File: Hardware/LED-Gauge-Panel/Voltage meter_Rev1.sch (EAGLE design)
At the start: 32 parts, among them J1 SL04, Q1 MOSFET-PCHANNEL, Q2 MOSFET-PCHANNEL, Q3 MOSFET-PCHANNEL, U1 ATMEGA328P_PDIPDIL28-4, U2 MAX232D, X1 22-23-2031, X2 16MHz

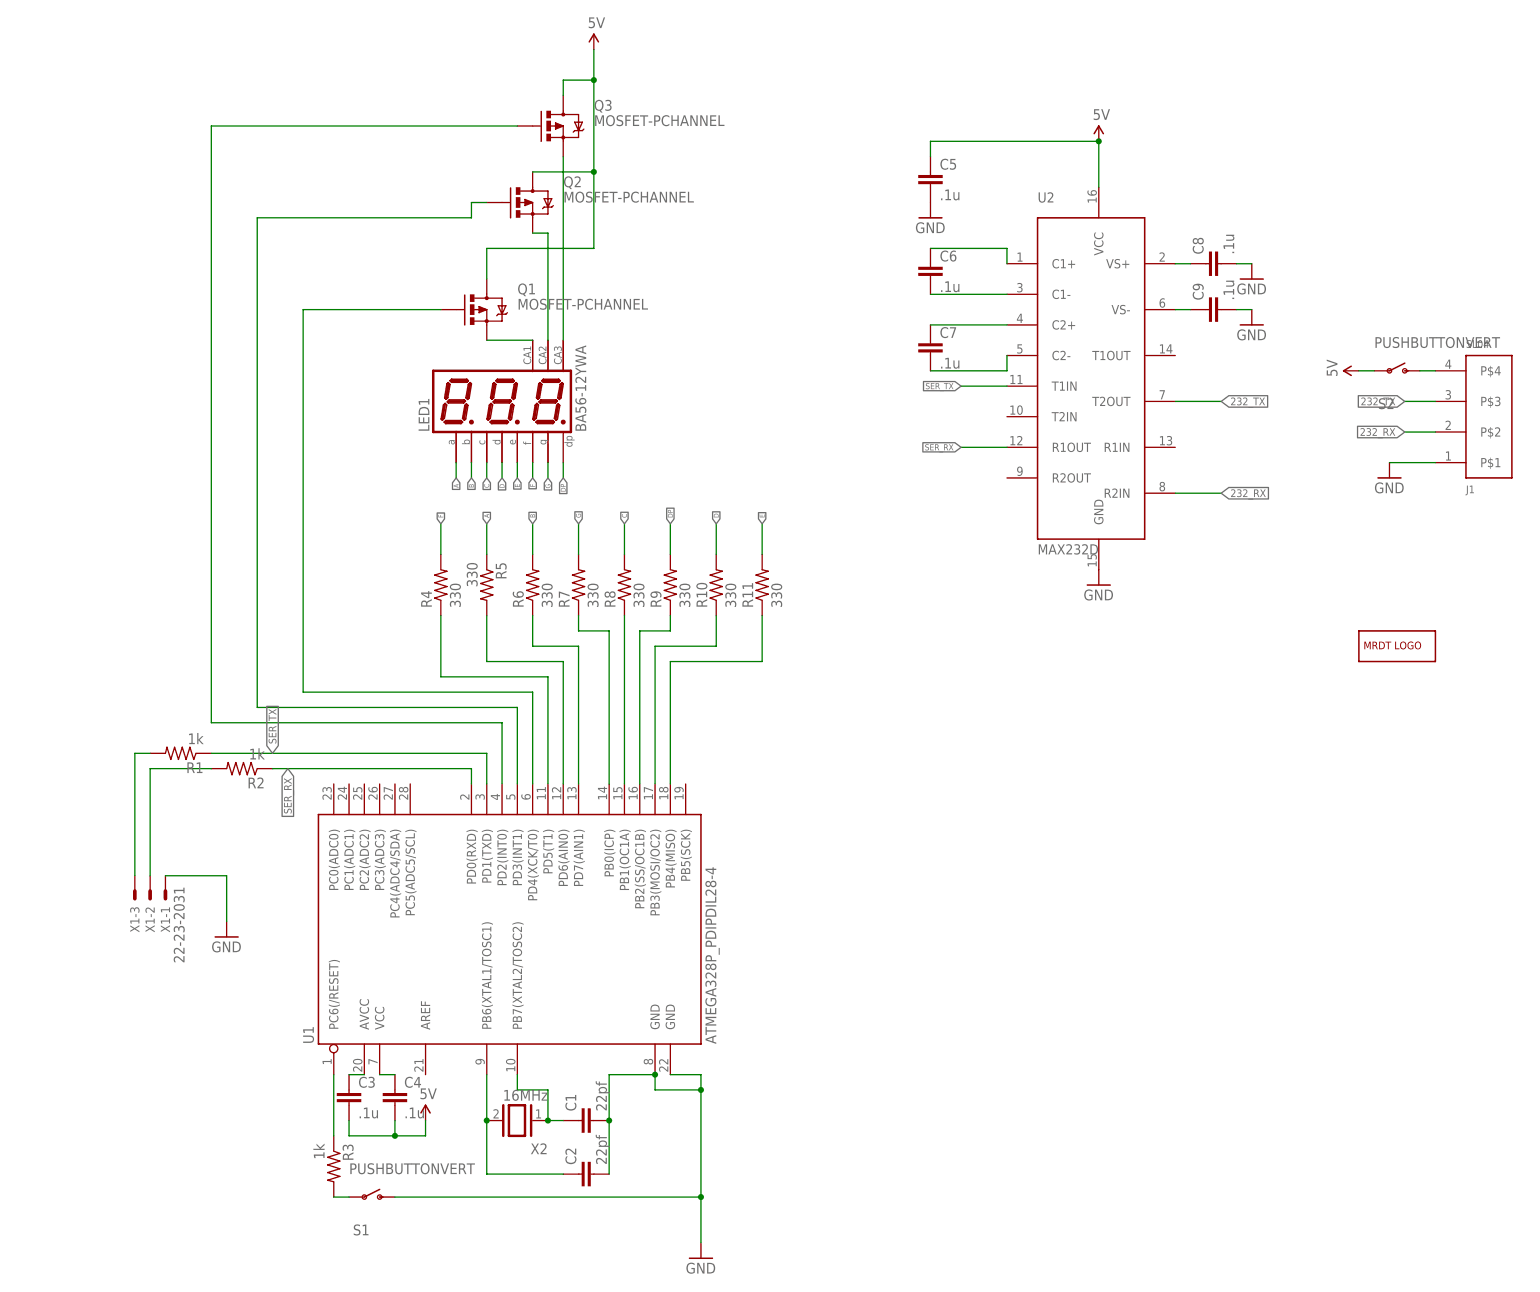
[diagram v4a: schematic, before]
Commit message: Final edits to Indicator Board
Small corrections- Moved some vias, added mounting holes, adjusted
sides.
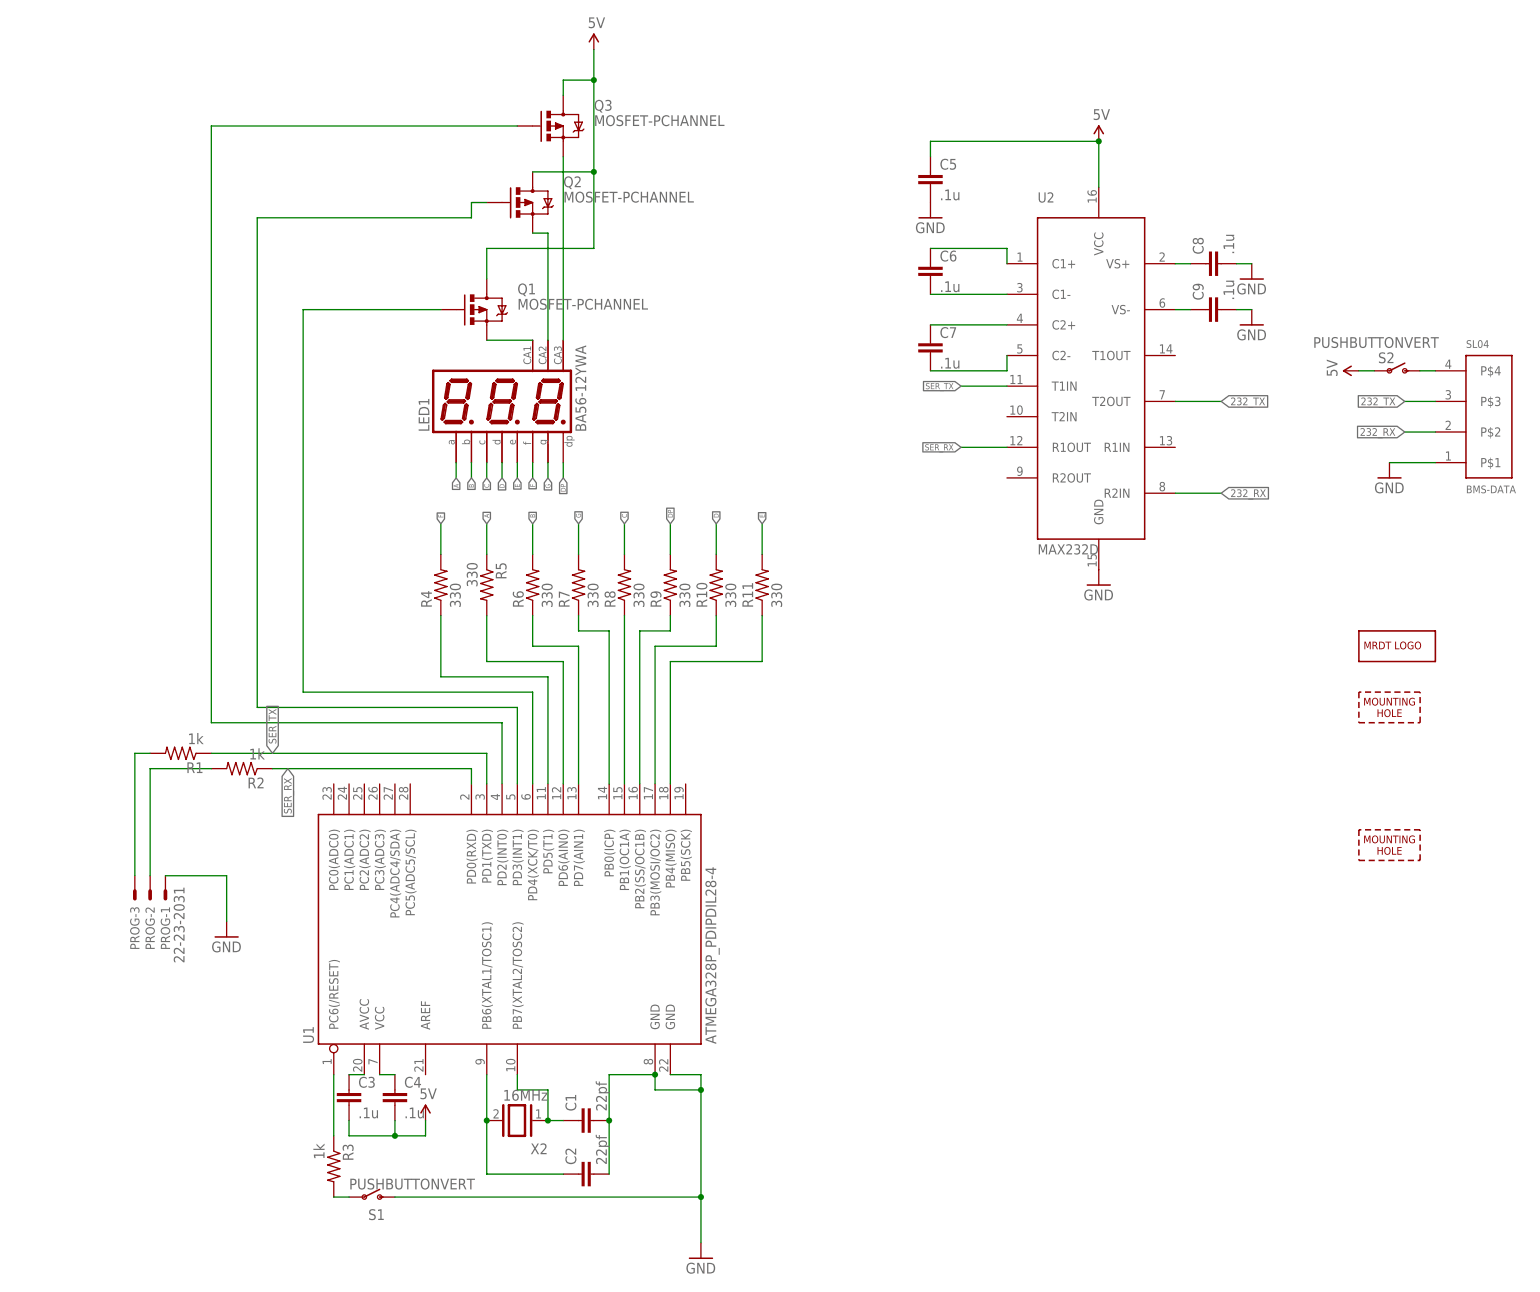
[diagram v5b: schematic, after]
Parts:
- added H1, H4: MOUNTING_HOLE#4, MRDT-Hardware:MOUNTING_HOLE#4
- renumbered J1 to BMS-DATA, X1 to PROG
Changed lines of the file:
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@@
 <?xml version="1.0" encoding="utf-8"?>
 <!DOCTYPE eagle SYSTEM "eagle.dtd">
-<eagle version="7.6.0">
+<eagle version="6.5.0">
 <drawing>
 <settings>
@@
 <part name="S2" library="MRDT-UserInput" deviceset="PUSHBUTTON" device="VERT"/>
 <part name="GND2" library="supply1" deviceset="GND" device=""/>
-<part name="J1" library="MRDT-Connectors" deviceset="SL04" device=""/>
+<part name="BMS-DATA" library="MRDT-Connectors" deviceset="SL04" device=""/>
 <part name="U2" library="MRDT-ICs" deviceset="MAX*232" device="D" value="MAX232D"/>
 <part name="C6" library="SparkFun-Passives" deviceset="CAP" device="0805" value=".1u"/>
@@
 <part name="R2" library="SparkFun-Passives" deviceset="RESISTOR" device="0805-RES" value="1k"/>
 <part name="GND5" library="supply1" deviceset="GND" device=""/>
-<part name="X1" library="con-molex" deviceset="22-23-2031" device=""/>
+<part name="PROG" library="con-molex" deviceset="22-23-2031" device=""/>
 <part name="X2" library="special" deviceset="XTAL/S" device="" value="16MHz"/>
 <part name="C2" library="SparkFun-Passives" deviceset="CAP" device="0805" value="22pf"/>
@@
 <part name="R3" library="SparkFun-Passives" deviceset="RESISTOR" device="0805-RES" value="1k"/>
 <part name="LOGO1" library="MRDT-Hardware" deviceset="MRDT_LOGO" device=""/>
+<part name="H1" library="MRDT-Hardware" deviceset="MOUNTING_HOLE" device="#4"/>
+<part name="H4" library="MRDT-Hardware" deviceset="MOUNTING_HOLE" device="#4"/>
 </parts>
 <sheets>
@@
 <instance part="R5" gate="G$1" x="20.32" y="-2.54" rot="R270"/>
 <instance part="R7" gate="G$1" x="35.56" y="-2.54" rot="R90"/>
-<instance part="S2" gate="G$1" x="170.18" y="33.02"/>
+<instance part="S2" gate="G$1" x="170.18" y="33.02" smashed="yes">
+<attribute name="NAME" x="168.275" y="34.29" size="1.778" layer="95"/>
+<attribute name="VALUE" x="157.48" y="36.83" size="1.778" layer="96"/>
+</instance>
 <instance part="GND2" gate="1" x="55.88" y="-114.3"/>
-<instance part="J1" gate="G$1" x="185.42" y="25.4" rot="MR180"/>
+<instance part="BMS-DATA" gate="G$1" x="185.42" y="25.4" rot="MR180"/>
 <instance part="U2" gate="G$1" x="121.92" y="33.02"/>
 <instance part="C6" gate="G$1" x="93.98" y="48.26"/>
@@
 <instance part="SUPPLY5" gate="G$1" x="38.1" y="86.36"/>
 <instance part="U1" gate="G$1" x="20.32" y="-60.96" rot="R90"/>
-<instance part="S1" gate="G$1" x="0" y="-104.14"/>
+<instance part="S1" gate="G$1" x="0" y="-104.14" smashed="yes">
+<attribute name="NAME" x="0.635" y="-107.95" size="1.778" layer="95"/>
+<attribute name="VALUE" x="-2.54" y="-102.87" size="1.778" layer="96"/>
+</instance>
 <instance part="SUPPLY1" gate="G$1" x="121.92" y="71.12"/>
 <instance part="R1" gate="G$1" x="-30.48" y="-30.48" rot="R180"/>
 <instance part="R2" gate="G$1" x="-20.32" y="-33.02" rot="R180"/>
 <instance part="GND5" gate="1" x="-22.86" y="-60.96"/>
-<instance part="X1" gate="-1" x="-33.02" y="-53.34" rot="R270"/>
-<instance part="X1" gate="-2" x="-35.56" y="-53.34" rot="R270"/>
-<instance part="X1" gate="-3" x="-38.1" y="-53.34" rot="R270"/>
+<instance part="PROG" gate="-1" x="-33.02" y="-53.34" rot="R270"/>
+<instance part="PROG" gate="-2" x="-35.56" y="-53.34" rot="R270"/>
+<instance part="PROG" gate="-3" x="-38.1" y="-53.34" rot="R270"/>
 <instance part="X2" gate="G$1" x="25.4" y="-91.44" rot="R180"/>
 <instance part="C2" gate="G$1" x="38.1" y="-100.33" rot="R90"/>
@@
 <instance part="R3" gate="G$1" x="-5.08" y="-99.06" rot="R270"/>
 <instance part="LOGO1" gate="G$1" x="165.1" y="-15.24"/>
+<instance part="H1" gate="G$1" x="165.1" y="-25.4"/>
+<instance part="H4" gate="G$1" x="165.1" y="-48.26"/>
 </instances>
 <busses>
@@
 <wire x1="177.8" y1="17.78" x2="170.18" y2="17.78" width="0.1524" layer="91"/>
 <pinref part="GND15" gate="1" pin="GND"/>
-<pinref part="J1" gate="G$1" pin="P$1"/>
+<pinref part="BMS-DATA" gate="G$1" pin="P$1"/>
 </segment>
 <segment>
@@
 <wire x1="-22.86" y1="-50.8" x2="-22.86" y2="-58.42" width="0.1524" layer="91"/>
 <pinref part="GND5" gate="1" pin="GND"/>
-<pinref part="X1" gate="-1" pin="S"/>
+<pinref part="PROG" gate="-1" pin="S"/>
 </segment>
 </net>
@@
 <wire x1="177.8" y1="22.86" x2="172.72" y2="22.86" width="0.1524" layer="91"/>
 <label x="172.72" y="22.86" size="1.27" layer="95" rot="R180" xref="yes"/>
-<pinref part="J1" gate="G$1" pin="P$2"/>
+<pinref part="BMS-DATA" gate="G$1" pin="P$2"/>
 </segment>
 <segment>
@@
 <wire x1="177.8" y1="27.94" x2="172.72" y2="27.94" width="0.1524" layer="91"/>
 <label x="172.72" y="27.94" size="1.27" layer="95" rot="R180" xref="yes"/>
-<pinref part="J1" gate="G$1" pin="P$3"/>
+<pinref part="BMS-DATA" gate="G$1" pin="P$3"/>
 </segment>
 </net>
@@
 <net name="N$7" class="0">
 <segment>
-<pinref part="J1" gate="G$1" pin="P$4"/>
+<pinref part="BMS-DATA" gate="G$1" pin="P$4"/>
 <pinref part="S2" gate="G$1" pin="S"/>
 <wire x1="175.26" y1="33.02" x2="177.8" y2="33.02" width="0.1524" layer="91"/>
@@
 <net name="N$14" class="0">
 <segment>
-<pinref part="X1" gate="-3" pin="S"/>
+<pinref part="PROG" gate="-3" pin="S"/>
 <wire x1="-38.1" y1="-30.48" x2="-38.1" y2="-50.8" width="0.1524" layer="91"/>
 <pinref part="R1" gate="G$1" pin="2"/>
@@
 <segment>
 <pinref part="R2" gate="G$1" pin="2"/>
-<pinref part="X1" gate="-2" pin="S"/>
+<pinref part="PROG" gate="-2" pin="S"/>
 <wire x1="-25.4" y1="-33.02" x2="-35.56" y2="-33.02" width="0.1524" layer="91"/>
 <wire x1="-35.56" y1="-33.02" x2="-35.56" y2="-50.8" width="0.1524" layer="91"/>
@@
 </schematic>
 </drawing>
+<compatibility>
+<note version="6.3" minversion="6.2.2" severity="warning">
+Since Version 6.2.2 text objects can contain more than one line,
+which will not be processed correctly with this version.
+</note>
+</compatibility>
 </eagle>

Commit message: Added signiture
Last edit before ordering
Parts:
- added U$1: JORDAN-NOWAK, sig:JORDAN-NOWAK
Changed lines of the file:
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@@
 <part name="H1" library="MRDT-Hardware" deviceset="MOUNTING_HOLE" device="#4"/>
 <part name="H4" library="MRDT-Hardware" deviceset="MOUNTING_HOLE" device="#4"/>
+<part name="U$1" library="sig" deviceset="JORDAN-NOWAK" device=""/>
 </parts>
 <sheets>
@@
 <instance part="C4" gate="G$1" x="5.08" y="-88.9"/>
 <instance part="R3" gate="G$1" x="-5.08" y="-99.06" rot="R270"/>
-<instance part="LOGO1" gate="G$1" x="165.1" y="-15.24"/>
+<instance part="LOGO1" gate="G$1" x="165.1" y="-17.78"/>
 <instance part="H1" gate="G$1" x="165.1" y="-25.4"/>
-<instance part="H4" gate="G$1" x="165.1" y="-48.26"/>
+<instance part="H4" gate="G$1" x="165.1" y="-33.02"/>
+<instance part="U$1" gate="G$1" x="165.1" y="-35.56"/>
 </instances>
 <busses>
